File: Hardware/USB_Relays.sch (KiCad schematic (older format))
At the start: 9 parts, among them J18 DNP, U2 PIC16F18854-SO

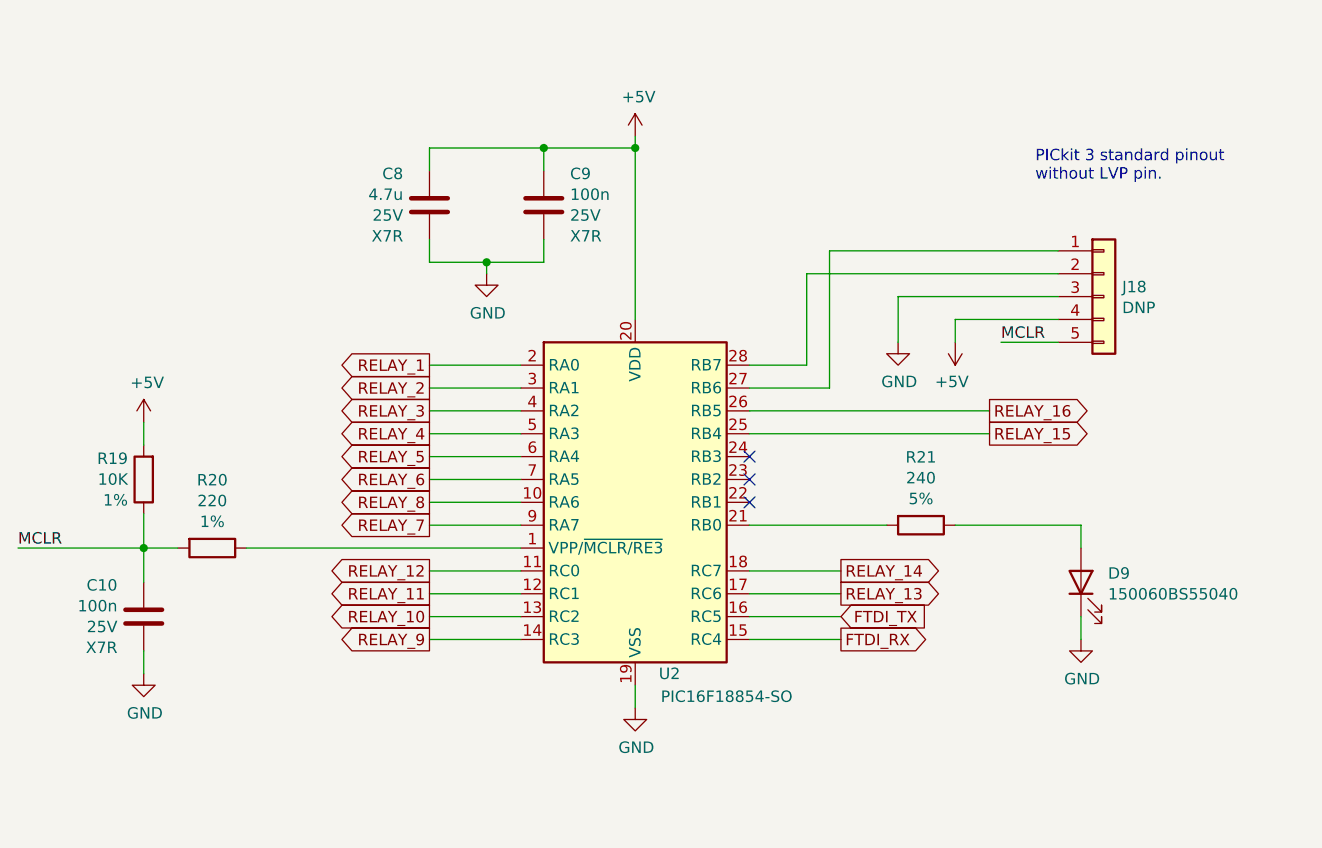
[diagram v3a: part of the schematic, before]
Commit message: [Hardware] Renamed components in a more coherent way.
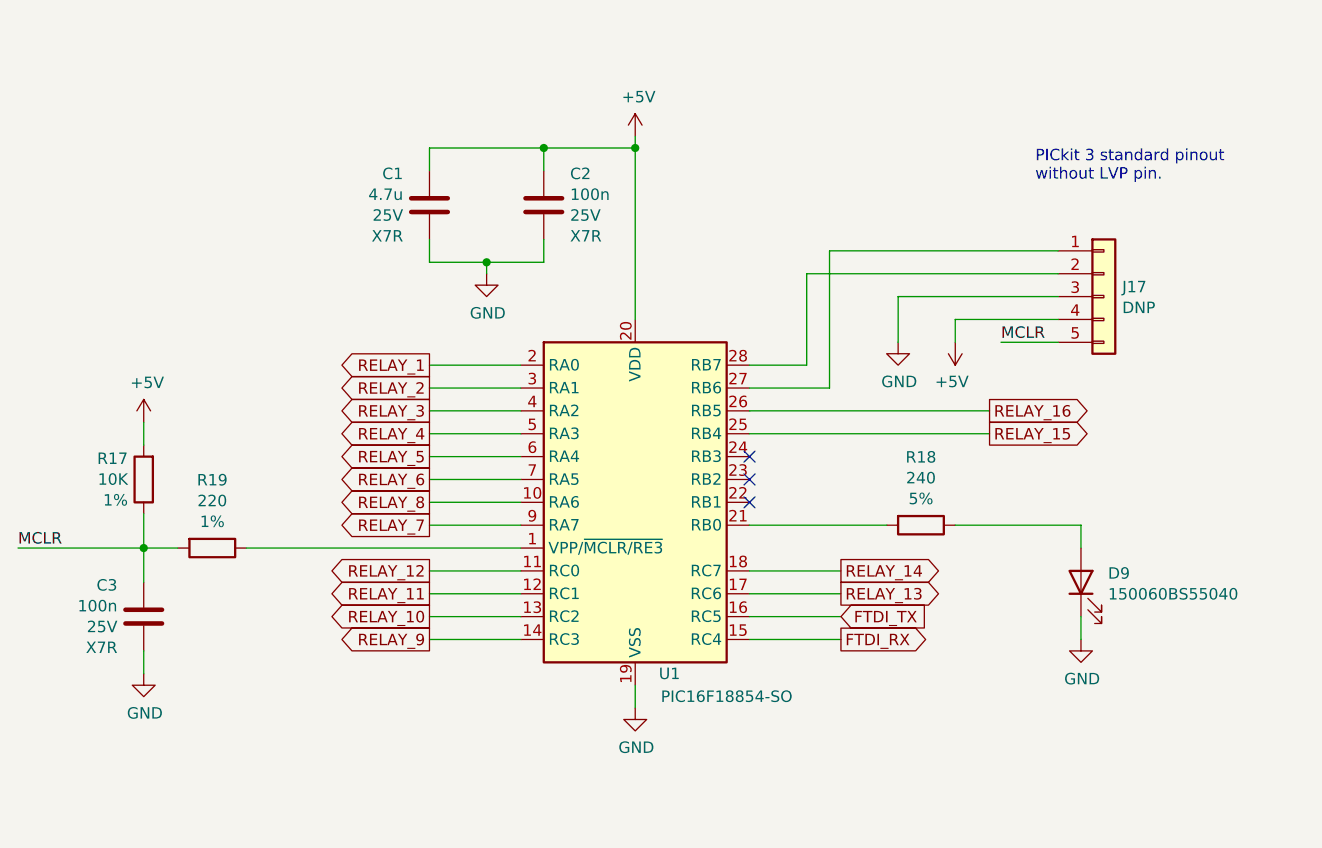
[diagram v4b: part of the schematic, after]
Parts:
- renumbered C8 to C1, C9 to C2, C10 to C3, J18 to J17, R19 to R17, R21 to R18, R20 to R19, U2 to U1
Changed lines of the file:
@@
 $EndSheet
 $Comp
-L MCU_Microchip_PIC16:PIC16F18854-SO U2
+L MCU_Microchip_PIC16:PIC16F18854-SO U1
 U 1 1 6170521F
 P 4300 3200
-F 0 "U2" H 4450 2450 50  0000 C CNN
+F 0 "U1" H 4450 2450 50  0000 C CNN
 F 1 "PIC16F18854-SO" H 4700 2350 50  0000 C CNN
 F 2 "Package_SO:SOIC-28W_7.5x17.9mm_P1.27mm" H 4300 2100 50  0001 C CNN
@@
 $EndComp
 $Comp
-L Connector_Generic:Conn_01x05 J18
+L Connector_Generic:Conn_01x05 J17
 U 1 1 6116AD75
 P 6350 2300
-F 0 "J18" H 6430 2342 50  0000 L CNN
+F 0 "J17" H 6430 2342 50  0000 L CNN
 F 1 "DNP" H 6430 2251 50  0000 L CNN
 F 2 "Connector_PinHeader_2.54mm:PinHeader_1x05_P2.54mm_Vertical" H 6350 2300 50  0001 C CNN
@@
 PICkit 3 standard pinout\nwithout LVP pin.
 $Comp
-L power:+5V #PWR038
+L power:+5V #PWR028
 U 1 1 6116F95E
 P 5700 2500
-F 0 "#PWR038" H 5700 2350 50  0001 C CNN
+F 0 "#PWR028" H 5700 2350 50  0001 C CNN
 F 1 "+5V" H 5715 2673 50  0000 C CNN
 F 2 "" H 5700 2500 50  0001 C CNN
@@
 $EndComp
 $Comp
-L power:GND #PWR037
+L power:GND #PWR027
 U 1 1 61170448
 P 5450 2500
-F 0 "#PWR037" H 5450 2250 50  0001 C CNN
+F 0 "#PWR027" H 5450 2250 50  0001 C CNN
 F 1 "GND" H 5455 2327 50  0000 C CNN
 F 2 "" H 5450 2500 50  0001 C CNN
@@
 	5700 2400 5700 2500
 $Comp
-L power:GND #PWR041
+L power:GND #PWR032
 U 1 1 61175030
 P 4300 4100
-F 0 "#PWR041" H 4300 3850 50  0001 C CNN
+F 0 "#PWR032" H 4300 3850 50  0001 C CNN
 F 1 "GND" H 4305 3927 50  0000 C CNN
 F 2 "" H 4300 4100 50  0001 C CNN
@@
 	4300 4100 4300 4000
 $Comp
-L power:+5V #PWR035
+L power:+5V #PWR025
 U 1 1 611761E2
 P 4300 1600
-F 0 "#PWR035" H 4300 1450 50  0001 C CNN
+F 0 "#PWR025" H 4300 1450 50  0001 C CNN
 F 1 "+5V" H 4315 1773 50  0000 C CNN
 F 2 "" H 4300 1600 50  0001 C CNN
@@
 	4300 2400 4300 1650
 $Comp
-L Device:C C8
+L Device:C C1
 U 1 1 6117A433
 P 3400 1900
-AR Path="/6117A433" Ref="C8"  Part="1"
+AR Path="/6117A433" Ref="C1"  Part="1"
 AR Path="/611612DA/6117A433" Ref="C?"  Part="1"
-F 0 "C8" H 3285 2037 50  0000 R CNN
+F 0 "C1" H 3285 2037 50  0000 R CNN
 F 1 "4.7u" H 3285 1946 50  0000 R CNN
 F 2 "Capacitor_SMD:C_0805_2012Metric_Pad1.18x1.45mm_HandSolder" H 3438 1750 50  0001 C CNN
@@
 $EndComp
 $Comp
-L Device:C C9
+L Device:C C2
 U 1 1 6117B1E3
 P 3900 1900
-AR Path="/6117B1E3" Ref="C9"  Part="1"
+AR Path="/6117B1E3" Ref="C2"  Part="1"
 AR Path="/611612DA/6117B1E3" Ref="C?"  Part="1"
-F 0 "C9" H 4015 2037 50  0000 L CNN
+F 0 "C2" H 4015 2037 50  0000 L CNN
 F 1 "100n" H 4015 1946 50  0000 L CNN
 F 2 "Capacitor_SMD:C_0603_1608Metric_Pad1.08x0.95mm_HandSolder" H 3938 1750 50  0001 C CNN
@@
 $EndComp
 $Comp
-L power:GND #PWR036
+L power:GND #PWR026
 U 1 1 6117F244
 P 3650 2200
-F 0 "#PWR036" H 3650 1950 50  0001 C CNN
+F 0 "#PWR026" H 3650 1950 50  0001 C CNN
 F 1 "GND" H 3655 2027 50  0000 C CNN
 F 2 "" H 3650 2200 50  0001 C CNN
@@
 MCLR
 $Comp
-L Device:R R20
+L Device:R R19
 U 1 1 611929BA
 P 2450 3400
-AR Path="/611929BA" Ref="R20"  Part="1"
+AR Path="/611929BA" Ref="R19"  Part="1"
 AR Path="/611612DA/611929BA" Ref="R?"  Part="1"
-F 0 "R20" V 2153 3400 50  0000 C CNN
+F 0 "R19" V 2153 3400 50  0000 C CNN
 F 1 "220" V 2244 3400 50  0000 C CNN
 F 2 "Resistor_SMD:R_0603_1608Metric_Pad0.98x0.95mm_HandSolder" V 2380 3400 50  0001 C CNN
@@
 $EndComp
 $Comp
-L Device:C C10
+L Device:C C3
 U 1 1 61192E0B
 P 2150 3700
-AR Path="/61192E0B" Ref="C10"  Part="1"
+AR Path="/61192E0B" Ref="C3"  Part="1"
 AR Path="/611612DA/61192E0B" Ref="C?"  Part="1"
-F 0 "C10" H 2035 3837 50  0000 R CNN
+F 0 "C3" H 2035 3837 50  0000 R CNN
 F 1 "100n" H 2035 3746 50  0000 R CNN
 F 2 "Capacitor_SMD:C_0603_1608Metric_Pad1.08x0.95mm_HandSolder" H 2188 3550 50  0001 C CNN
@@
 $EndComp
 $Comp
-L Device:R R19
+L Device:R R17
 U 1 1 6119490A
 P 2150 3100
-AR Path="/6119490A" Ref="R19"  Part="1"
+AR Path="/6119490A" Ref="R17"  Part="1"
 AR Path="/611612DA/6119490A" Ref="R?"  Part="1"
-F 0 "R19" H 2219 3009 50  0000 L CNN
+F 0 "R17" H 2219 3009 50  0000 L CNN
 F 1 "10K" H 2219 3100 50  0000 L CNN
 F 2 "Resistor_SMD:R_0603_1608Metric_Pad0.98x0.95mm_HandSolder" V 2080 3100 50  0001 C CNN
@@
 $EndComp
 $Comp
-L power:GND #PWR040
+L power:GND #PWR031
 U 1 1 6119B79A
 P 2150 3950
-F 0 "#PWR040" H 2150 3700 50  0001 C CNN
+F 0 "#PWR031" H 2150 3700 50  0001 C CNN
 F 1 "GND" H 2155 3777 50  0000 C CNN
 F 2 "" H 2150 3950 50  0001 C CNN
@@
 $EndComp
 $Comp
-L power:+5V #PWR039
+L power:+5V #PWR029
 U 1 1 6119BBA3
 P 2150 2850
-F 0 "#PWR039" H 2150 2700 50  0001 C CNN
+F 0 "#PWR029" H 2150 2700 50  0001 C CNN
 F 1 "+5V" H 2165 3023 50  0000 C CNN
 F 2 "" H 2150 2850 50  0001 C CNN
@@
 $EndComp
 $Comp
-L power:GND #PWR0101
+L power:GND #PWR030
 U 1 1 61211B07
 P 6250 3800
-F 0 "#PWR0101" H 6250 3550 50  0001 C CNN
+F 0 "#PWR030" H 6250 3550 50  0001 C CNN
 F 1 "GND" H 6255 3627 50  0000 C CNN
 F 2 "" H 6250 3800 50  0001 C CNN
@@
 	6250 3800 6250 3700
 $Comp
-L Device:R R21
+L Device:R R18
 U 1 1 61213BD6
 P 5550 3300
-F 0 "R21" V 5253 3300 50  0000 C CNN
+F 0 "R18" V 5253 3300 50  0000 C CNN
 F 1 "240" V 5344 3300 50  0000 C CNN
 F 2 "Resistor_SMD:R_1206_3216Metric_Pad1.30x1.75mm_HandSolder" V 5480 3300 50  0001 C CNN

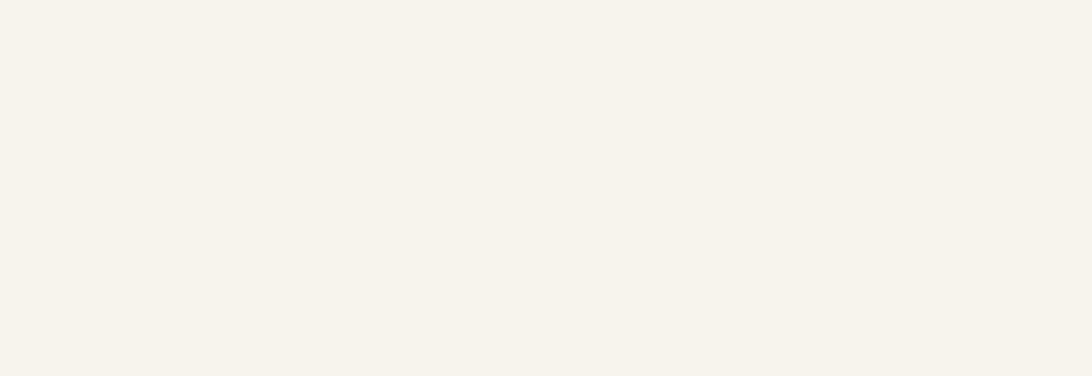
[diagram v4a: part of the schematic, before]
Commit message: [Hardware] Added mounting holes, PCB contour and ground planes.
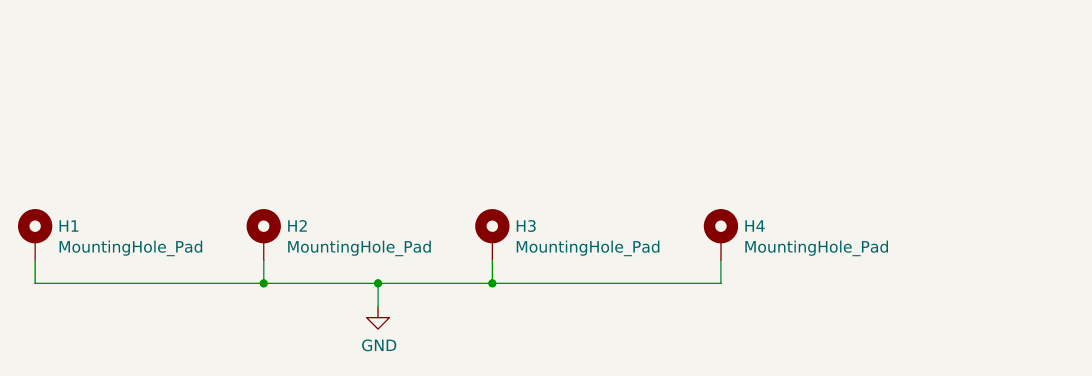
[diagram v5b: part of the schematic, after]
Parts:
- added H1, H2, H3, H4: MountingHole_Pad, MountingHole:MountingHole_4.5mm_Pad, symbol Mechanical:MountingHole_Pad
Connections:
- net GND: now also H1.1, H2.1, H3.1, H4.1
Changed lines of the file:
@@
 Wire Wire Line
 	6250 3300 6250 3400
+$Comp
+L Mechanical:MountingHole_Pad H2
+U 1 1 6117A771
+P 2000 5550
+F 0 "H2" H 2100 5599 50  0000 L CNN
+F 1 "MountingHole_Pad" H 2100 5508 50  0000 L CNN
+F 2 "MountingHole:MountingHole_4.5mm_Pad" H 2000 5550 50  0001 C CNN
+F 3 "~" H 2000 5550 50  0001 C CNN
+	1    2000 5550
+	1    0    0    -1
+$EndComp
+$Comp
+L Mechanical:MountingHole_Pad H1
+U 1 1 6117AF37
+P 1000 5550
+F 0 "H1" H 1100 5599 50  0000 L CNN
+F 1 "MountingHole_Pad" H 1100 5508 50  0000 L CNN
+F 2 "MountingHole:MountingHole_4.5mm_Pad" H 1000 5550 50  0001 C CNN
+F 3 "~" H 1000 5550 50  0001 C CNN
+	1    1000 5550
+	1    0    0    -1
+$EndComp
+$Comp
+L Mechanical:MountingHole_Pad H3
+U 1 1 6117C2B5
+P 3000 5550
+F 0 "H3" H 3100 5599 50  0000 L CNN
+F 1 "MountingHole_Pad" H 3100 5508 50  0000 L CNN
+F 2 "MountingHole:MountingHole_4.5mm_Pad" H 3000 5550 50  0001 C CNN
+F 3 "~" H 3000 5550 50  0001 C CNN
+	1    3000 5550
+	1    0    0    -1
+$EndComp
+$Comp
+L Mechanical:MountingHole_Pad H4
+U 1 1 6117C5A4
+P 4000 5550
+F 0 "H4" H 4100 5599 50  0000 L CNN
+F 1 "MountingHole_Pad" H 4100 5508 50  0000 L CNN
+F 2 "MountingHole:MountingHole_4.5mm_Pad" H 4000 5550 50  0001 C CNN
+F 3 "~" H 4000 5550 50  0001 C CNN
+	1    4000 5550
+	1    0    0    -1
+$EndComp
+Wire Wire Line
+	1000 5650 1000 5750
+Wire Wire Line
+	1000 5750 2000 5750
+Wire Wire Line
+	2000 5750 2000 5650
+Wire Wire Line
+	2000 5750 2500 5750
+Wire Wire Line
+	3000 5750 3000 5650
+Connection ~ 2000 5750
+Wire Wire Line
+	3000 5750 4000 5750
+Wire Wire Line
+	4000 5750 4000 5650
+Connection ~ 3000 5750
+$Comp
+L power:GND #PWR043
+U 1 1 6117FD7B
+P 2500 5850
+F 0 "#PWR043" H 2500 5600 50  0001 C CNN
+F 1 "GND" H 2505 5677 50  0000 C CNN
+F 2 "" H 2500 5850 50  0001 C CNN
+F 3 "" H 2500 5850 50  0001 C CNN
+	1    2500 5850
+	1    0    0    -1
+$EndComp
+Wire Wire Line
+	2500 5850 2500 5750
+Connection ~ 2500 5750
+Wire Wire Line
+	2500 5750 3000 5750
 $EndSCHEMATC

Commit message: [Hardware] Routed whole PCB.
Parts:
- D9: footprint LED_SMD:LED_0201_0603Metric_Pad0.64x0.40mm_HandSolder -> LED_SMD:LED_0603_1608Metric_Pad1.05x0.95mm_HandSolder
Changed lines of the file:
@@
 F 0 "D9" V 6289 3432 50  0000 R CNN
 F 1 "150060BS55040" V 6198 3432 50  0000 R CNN
-F 2 "LED_SMD:LED_0201_0603Metric_Pad0.64x0.40mm_HandSolder" H 6250 3550 50  0001 C CNN
+F 2 "LED_SMD:LED_0603_1608Metric_Pad1.05x0.95mm_HandSolder" H 6250 3550 50  0001 C CNN
 F 3 "~" H 6250 3550 50  0001 C CNN
 F 4 "Wurth" H 6250 3550 50  0001 C CNN "Manufacturer"

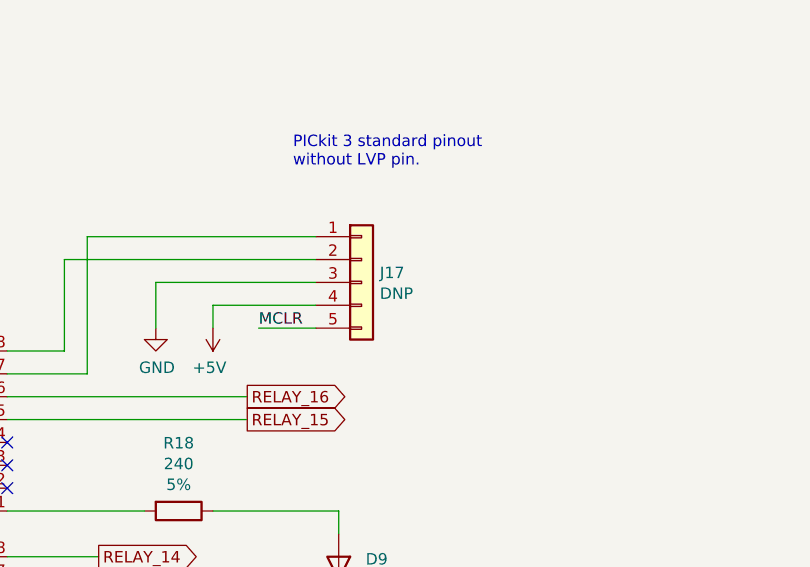
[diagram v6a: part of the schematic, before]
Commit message: [Hardware] Improved bill of materials generation.
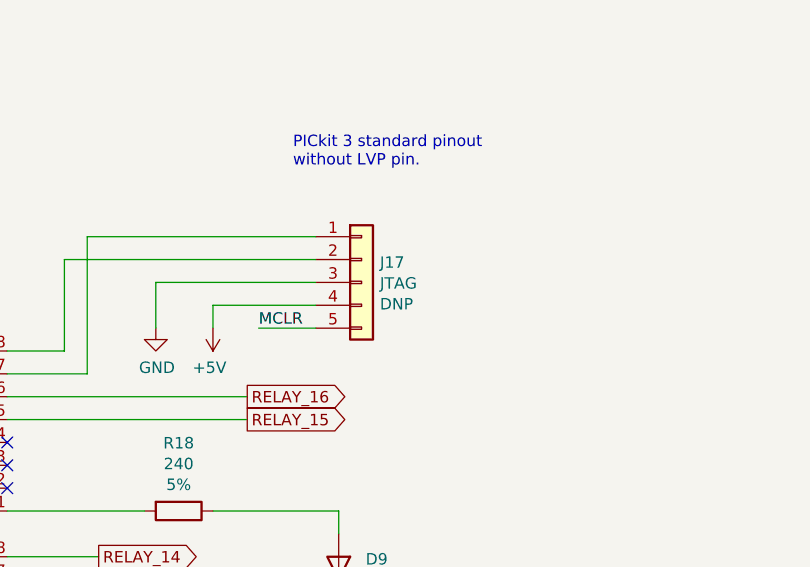
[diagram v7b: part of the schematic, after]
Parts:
- H1, H2, H3, H4: Populate (none) -> DNP
- J17: value DNP -> JTAG; Populate (none) -> DNP
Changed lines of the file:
@@
 U 1 1 6116AD75
 P 6350 2300
-F 0 "J17" H 6430 2342 50  0000 L CNN
-F 1 "DNP" H 6430 2251 50  0000 L CNN
+F 0 "J17" H 6430 2387 50  0000 L CNN
+F 1 "JTAG" H 6430 2296 50  0000 L CNN
 F 2 "Connector_PinHeader_2.54mm:PinHeader_1x05_P2.54mm_Vertical" H 6350 2300 50  0001 C CNN
 F 3 "~" H 6350 2300 50  0001 C CNN
+F 4 "DNP" H 6430 2205 50  0000 L CNN "Populate"
 	1    6350 2300
 	1    0    0    -1
@@
 F 2 "MountingHole:MountingHole_4.5mm_Pad" H 2000 5550 50  0001 C CNN
 F 3 "~" H 2000 5550 50  0001 C CNN
+F 4 "DNP" H 2000 5550 50  0001 C CNN "Populate"
 	1    2000 5550
 	1    0    0    -1
@@
 F 2 "MountingHole:MountingHole_4.5mm_Pad" H 1000 5550 50  0001 C CNN
 F 3 "~" H 1000 5550 50  0001 C CNN
+F 4 "DNP" H 1000 5550 50  0001 C CNN "Populate"
 	1    1000 5550
 	1    0    0    -1
@@
 F 2 "MountingHole:MountingHole_4.5mm_Pad" H 3000 5550 50  0001 C CNN
 F 3 "~" H 3000 5550 50  0001 C CNN
+F 4 "DNP" H 3000 5550 50  0001 C CNN "Populate"
 	1    3000 5550
 	1    0    0    -1
@@
 F 2 "MountingHole:MountingHole_4.5mm_Pad" H 4000 5550 50  0001 C CNN
 F 3 "~" H 4000 5550 50  0001 C CNN
+F 4 "DNP" H 4000 5550 50  0001 C CNN "Populate"
 	1    4000 5550
 	1    0    0    -1
